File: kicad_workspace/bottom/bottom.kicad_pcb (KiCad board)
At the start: 2 copper layers, 76.8 x 84 mm, 64 parts, among them J1 Battery connector, J2 Battery connector, M1 N20_MOTOR_EXTENDED_SHAFT, M2 N20_MOTOR_EXTENDED_SHAFT, U1 DRV8833PWP, U12 ACS712-5A, U13 ACS712-5A, U3 STM32F303RETx, U4 BNO055, Y1 32.768kHz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

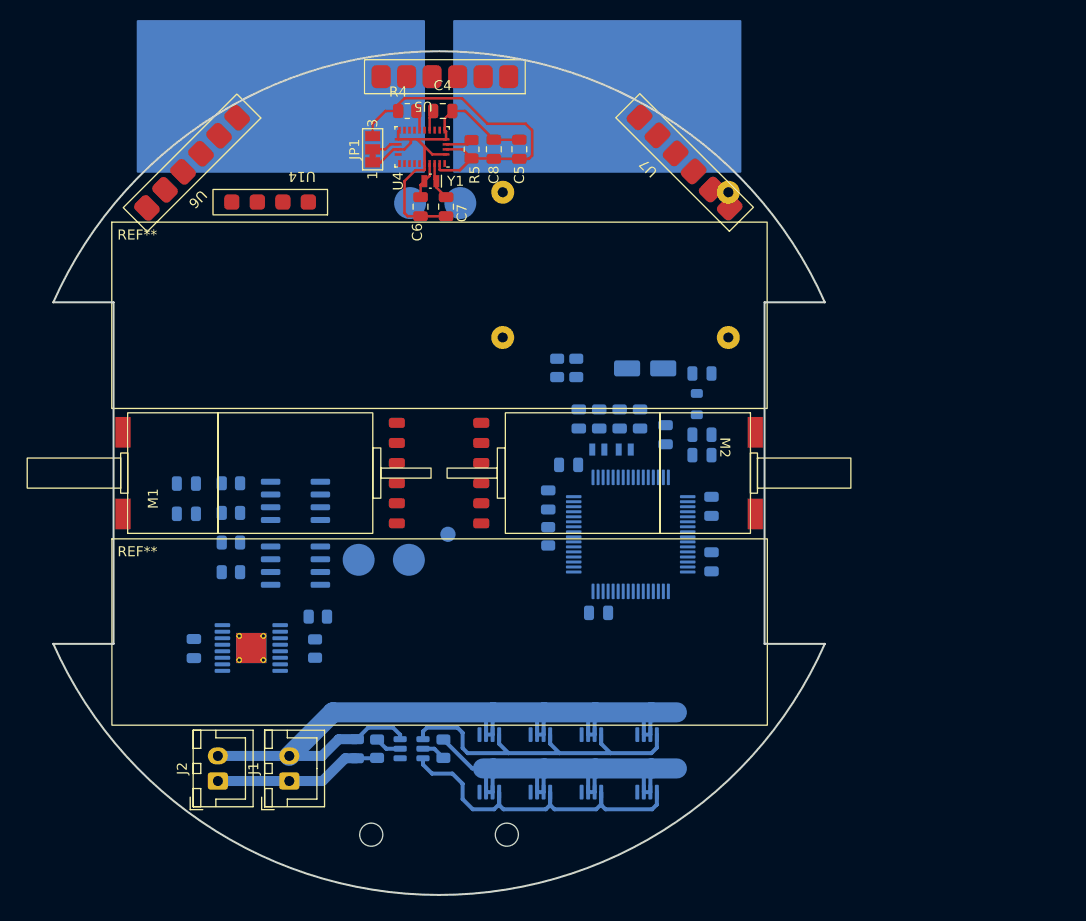
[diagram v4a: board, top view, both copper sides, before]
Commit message: changed tp5100 footprint to smd. add wiring for li-ion protection and charging
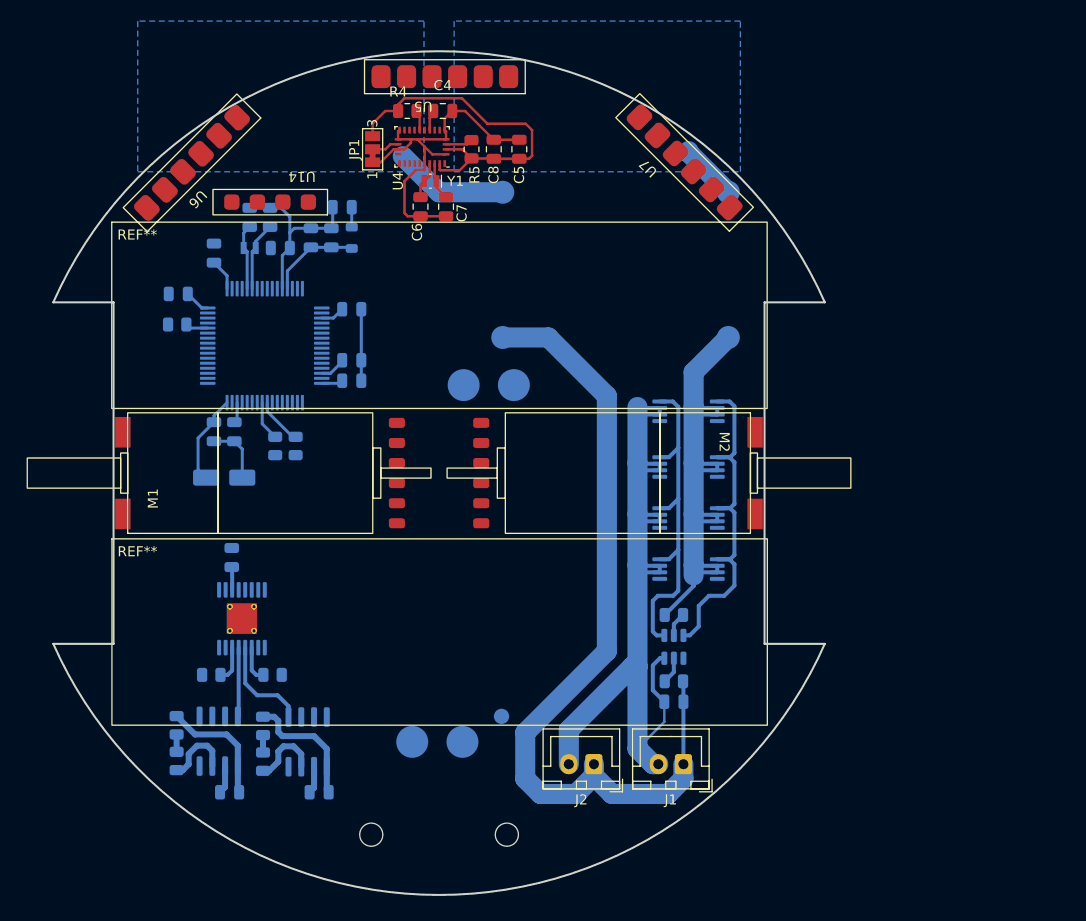
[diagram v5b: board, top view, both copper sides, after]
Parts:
- removed C20, C21: 4.3pF, Capacitor_SMD:C_0805_2012Metric
- removed U3: STM32F303RETx, Package_QFP:LQFP-64_10x10mm_P0.5mm
- removed Y3: 32.768kHz, Crystal:Crystal_SMD_MicroCrystal_CM9V-T1A-2Pin_1.6x1.0mm
- added C24: 2.2uF, Capacitor_SMD:C_0805_2012Metric, B.Cu at (51.3, 48.8)
- added C25: 2.2uF, Capacitor_SMD:C_0805_2012Metric, B.Cu at (39.6, 55.9)
- added U17: STM32H7A3RITx, Package_QFP:LQFP-64_10x10mm_P0.5mm, B.Cu at (42.6, 47.3)
- moved C12 52.4 mm to (37.6, 38.1), turned to 90 degrees
- moved C17 44.5 mm to (47.2, 36.6), turned to 90 degrees
- moved C3 43.3 mm to (38.6, 60.5), turned to 0 degrees
- moved C10 42.6 mm to (44.2, 37.6), turned to 0 degrees
- moved R3 42.5 mm to (33.9, 45.2), turned to 180 degrees
- moved C11 42.4 mm to (34.0, 42.2)
- moved Y2 42.4 mm to (41.1, 37.6)
- moved C18 41.9 mm to (43.2, 34.5)
- moved C19 41.9 mm to (41.1, 34.5)
- moved C16 41.8 mm to (49.3, 36.6), turned to 90 degrees
- moved C14 40.8 mm to (51.3, 43.7), turned to 0 degrees
- moved C13 40.1 mm to (51.3, 50.8), turned to 0 degrees
- moved C2 39.5 mm to (50.4, 33.5), turned to 180 degrees
- moved J1 39.3 mm to (84.3, 89.0), turned to 180 degrees
- moved FB1 38.1 mm to (51.3, 36.6)
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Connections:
- U13 pad 1: IP_MOTOR_A+ -> IP_MOTOR_A-
- U13 pad 2: IP_MOTOR_A+ -> IP_MOTOR_A-
- U13 pad 3: IP_MOTOR_A- -> IP_MOTOR_A+
- U13 pad 4: IP_MOTOR_A- -> IP_MOTOR_A+
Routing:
- net +BATT: track 16.8 -> 83.6 mm
- net -BATT_PROT: track 85.1 -> 147.0 mm
- net +3.3V: track 35.8 -> 57.0 mm
- net VIN_PAD+: track 0.00 -> 11.4 mm
- net IP_MOTOR_A-: track 0.00 -> 9.88 mm
- net +3.3VA: track 0.00 -> 9.20 mm
- net Net-(U13-VIOUT): track 0.00 -> 7.00 mm
- net Net-(U12-VIOUT): track 0.00 -> 6.89 mm
- net Net-(U17-PH1): track 0.00 -> 6.88 mm
- net IP_MOTOR_B-: track 0.00 -> 6.88 mm
- net Net-(U17-PH0): track 0.00 -> 6.54 mm
- net VIN_PAD-: track 0.00 -> 5.74 mm
- net SDA: track 0.00 -> 4.75 mm
- net SCL: track 0.00 -> 3.93 mm
- net Net-(U1-BISEN): track 0.00 -> 3.61 mm
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- added copper zone on B.Cu, net VIN_PAD+
- added copper zone on B.Cu, net VIN_PAD-

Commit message: wired motors
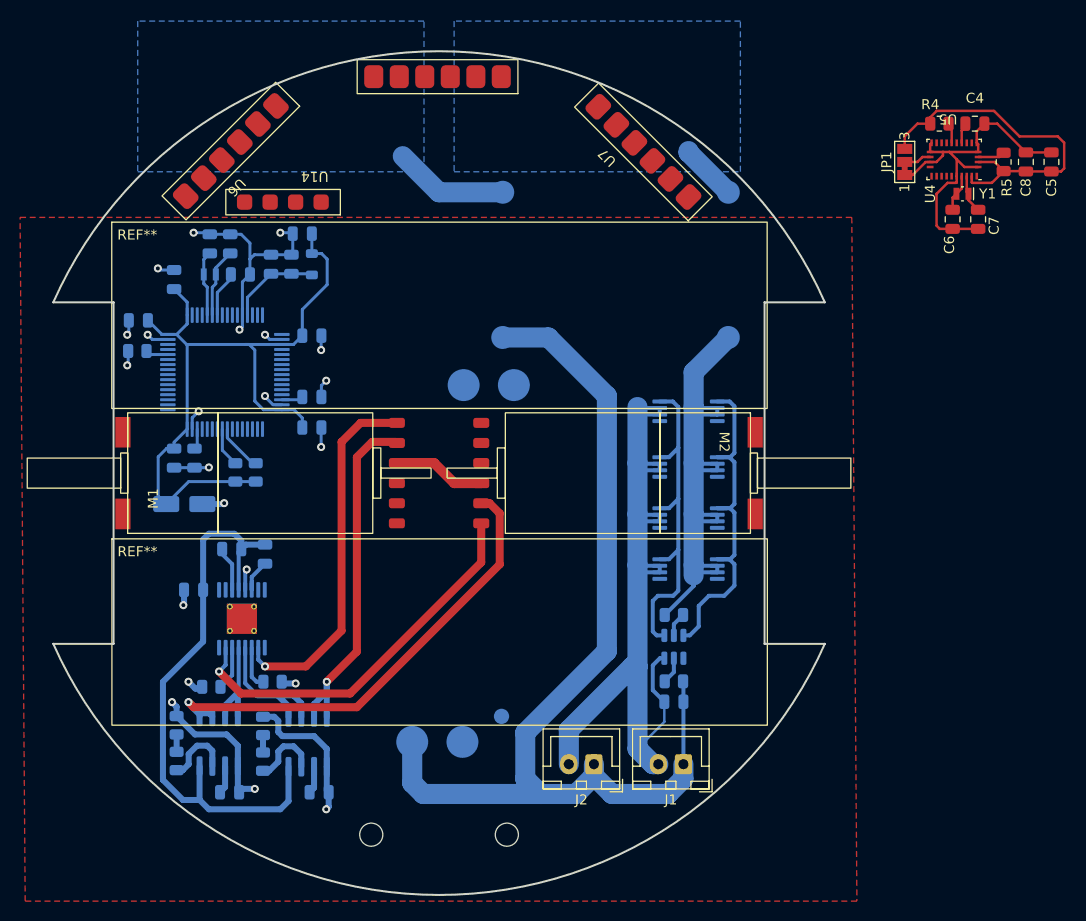
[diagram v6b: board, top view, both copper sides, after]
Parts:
- added C20: 2.2uF, Capacitor_SMD:C_0805_2012Metric, B.Cu at (42.7, 68.1)
- added C21: 2.2uF, Capacitor_SMD:C_0805_2012Metric, B.Cu at (35.6, 71.6)
- moved C5 53.0 mm to (121.0, 29.0)
- moved C7 53.0 mm to (113.7, 34.7)
- moved C4 53.0 mm to (113.3, 25.2)
- moved C6 53.0 mm to (111.1, 34.7)
- moved JP1 53.0 mm to (106.4, 29.0)
- moved R4 53.0 mm to (109.8, 25.2)
- moved R5 53.0 mm to (116.2, 29.0)
- moved U4 53.0 mm to (111.3, 28.8)
- moved Y1 53.0 mm to (112.1, 32.2)
- moved C8 53.0 mm to (118.4, 29.0)
- moved C13 6.13 mm to (47.3, 55.5)
- moved C24 5.39 mm to (47.3, 52.4)
- moved C18 4.76 mm to (39.2, 37.2)
- moved C19 4.76 mm to (37.2, 37.2)
- moved C10 4.76 mm to (40.2, 40.2)
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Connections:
- net /NRST renamed NRST
- net Net-(M1-M1) renamed /MOTOR_A-
- net Net-(M2-M1) renamed /MOTOR_B-
- U1 pad 1: unconnected-(U1-nSLEEP-Pad1) -> DRV_SLEEP
- U1 pad 14: +3.3V -> Net-(U1-VINT)
- U1 pad 8: unconnected-(U1-nFAULT-Pad8) -> DRV_FAULT
- U17 pad 45: unconnected-(U17-PA13-Pad45) -> SWDIO
- U17 pad 49: unconnected-(U17-PA14-Pad49) -> SWCLK
- U17 pad 55: unconnected-(U17-PB3-Pad55) -> SWO
- U5 pad 5: unconnected-(U5-GPIO1-Pad5) -> VL_IRQ1
- U6 pad 5: unconnected-(U6-GPIO1-Pad5) -> VL_IRQ2
- U7 pad 5: unconnected-(U7-GPIO1-Pad5) -> VL_IRQ3
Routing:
- net +3.3V: track 57.0 -> 120.0 mm
- net +5V: track 0.00 -> 58.3 mm
- net IP_MOTOR_B+: track 0.00 -> 47.7 mm, vias 0 -> 1
- net /MOTOR_B-: track 0.00 -> 39.0 mm, vias 0 -> 1
- net /MOTOR_A-: track 0.00 -> 36.3 mm, vias 0 -> 1
- net IP_MOTOR_A+: track 0.00 -> 35.8 mm, vias 0 -> 1
- net -BATT_PROT: track 147.0 -> 173.6 mm, vias 0 -> 22
- net +BATT: track 83.6 -> 100.9 mm
- net NRST: track 0.00 -> 4.61 mm
- net IP_MOTOR_A-: track 9.88 -> 13.9 mm
- net Net-(U1-VINT): track 0.00 -> 3.99 mm
- net IP_MOTOR_B-: track 6.88 -> 9.87 mm
- net Net-(U1-VCP): track 2.29 -> 3.97 mm
- net Net-(U1-BISEN): track 3.61 -> 4.38 mm
- net Net-(U1-AISEN): track 3.61 -> 4.27 mm
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- added copper zone on F.Cu, net -BATT_PROT

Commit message: prepare to wire distance sensors
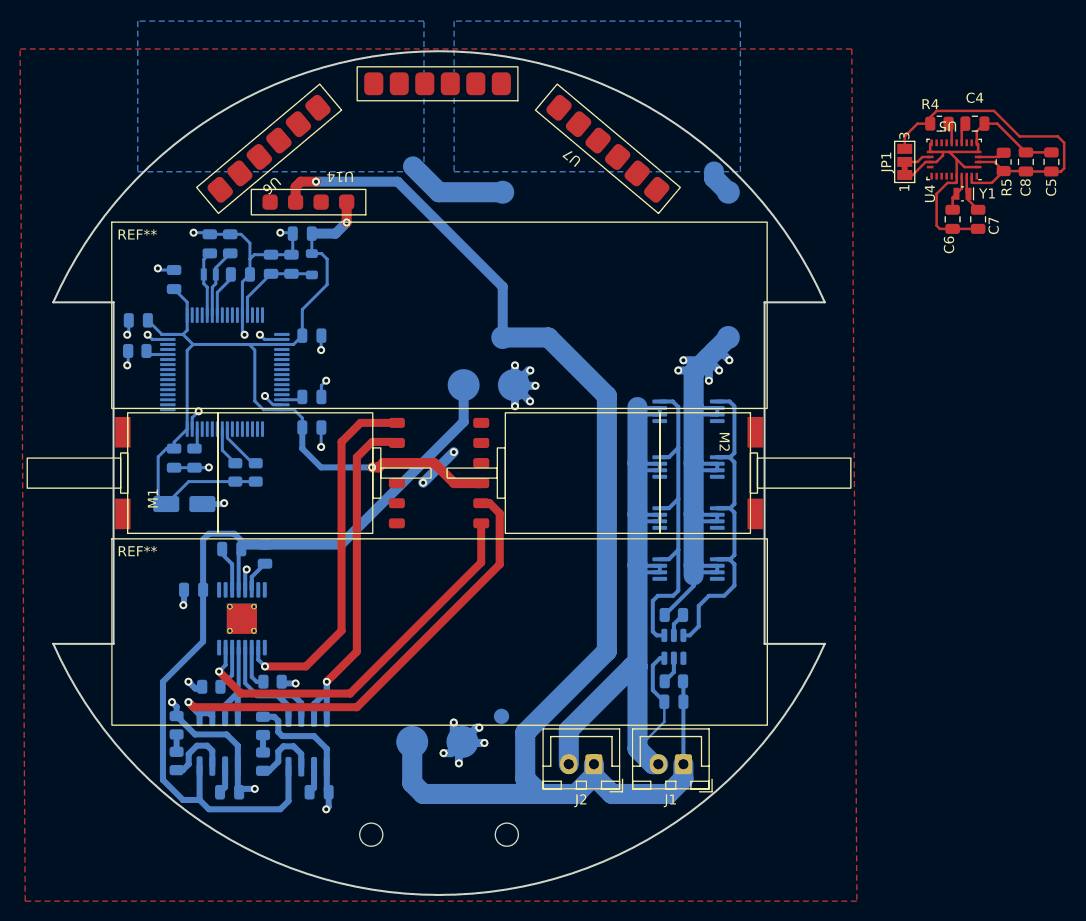
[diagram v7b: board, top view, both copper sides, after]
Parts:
- moved U6 4.19 mm to (50.3, 23.9), turned to -140 degrees
- moved U7 3.04 mm to (81.9, 34.1), turned to 140 degrees
- moved U14 2.54 mm to (52.7, 34.3)
- moved U5 0.71 mm to (67.8, 22.9)
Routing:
- net -BATT_PROT: track 173.6 -> 212.8 mm, vias 22 -> 39
- net +BATT: track 100.9 -> 132.7 mm, vias 0 -> 1
- net +5V: track 58.3 -> 86.8 mm
- net +3.3V: track 120.0 -> 139.2 mm, vias 0 -> 2
- net VIN_PAD-: track 5.74 -> 2.66 mm
- net VIN_PAD+: track 11.4 -> 10.0 mm

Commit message: wired laser sensors
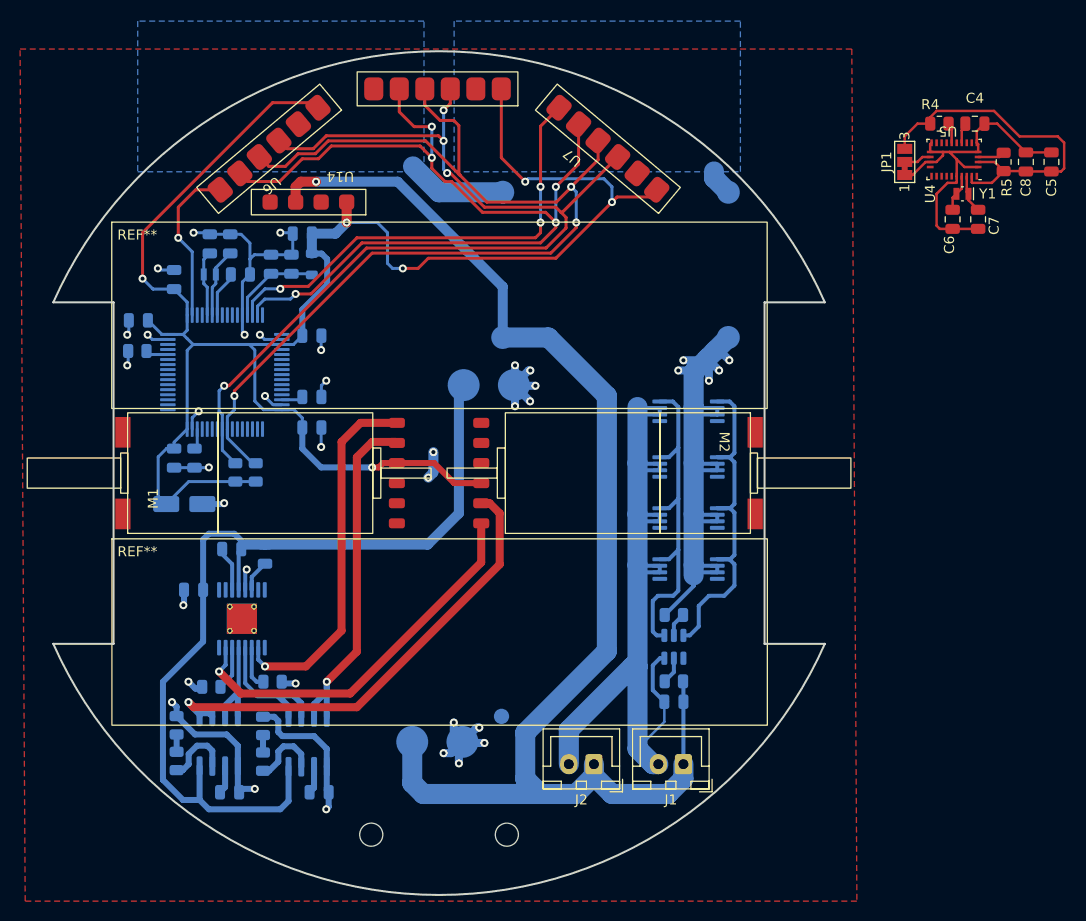
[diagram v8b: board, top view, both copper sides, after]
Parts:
- moved U5 0.51 mm to (67.8, 23.4)
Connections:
- U17 pad 14: unconnected-(U17-PA0-Pad14) -> VL_EN3
- U17 pad 15: unconnected-(U17-PA1-Pad15) -> VL_IRQ
- U17 pad 2: unconnected-(U17-PC13-Pad2) -> VL_EN2
- U5 pad 5: VL_IRQ1 -> VL_IRQ
- U6 pad 5: VL_IRQ2 -> VL_IRQ
- U7 pad 5: VL_IRQ3 -> VL_IRQ
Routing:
- net SDA: track 4.75 -> 106.6 mm, vias 0 -> 3
- net SCL: track 3.93 -> 98.6 mm, vias 0 -> 4
- net VL_IRQ: track 0.00 -> 91.8 mm, vias 0 -> 5
- net +3.3V: track 139.2 -> 229.5 mm, vias 2 -> 6
- net VL_EN3: track 0.00 -> 46.1 mm, vias 0 -> 3
- net VL_EN2: track 0.00 -> 16.2 mm, vias 0 -> 1
- net +5V: track 86.8 -> 91.9 mm
- net -BATT_PROT: track 212.8 -> 211.4 mm
